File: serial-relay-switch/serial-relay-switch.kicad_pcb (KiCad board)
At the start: 2 copper layers, 170.2 x 66 mm, 75 parts, among them J1 Screw_Terminal_01x01, J10 Screw_Terminal_01x01, J11 Screw_Terminal_01x01, J17 Conn_01x01, J18 Conn_01x01, J19 Screw_Terminal_01x01, J2 2501551-4, J20 Screw_Terminal_01x01, J21 Conn_01x01, J4 Screw_Terminal_01x01, J5 Screw_Terminal_01x01, J6 Screw_Terminal_01x01, J7 Screw_Terminal_01x01, J8 Screw_Terminal_01x01, J9 Screw_Terminal_01x01, K1 G2RL-1-E, K2 G2RL-1-E, K3 G2RL-1-E, K4 G2RL-1-E, K5 G2RL-1-E, K6 G2RL-1-E, K7 G2RL-1-E, K8 G2RL-1-E, U1 H11L1, U13 STM1810T, U14 74LVC1G32, U15 74LVC1G08, U16 74LVC1G04, U17 74LS163, U2 ISL8488E, U3 SZNUD3124DMT1G, U4 ISL8488E, U5 74HC594, U6 SZNUD3124DMT1G, U7 SZNUD3124DMT1G, U8 SZNUD3124DMT1G

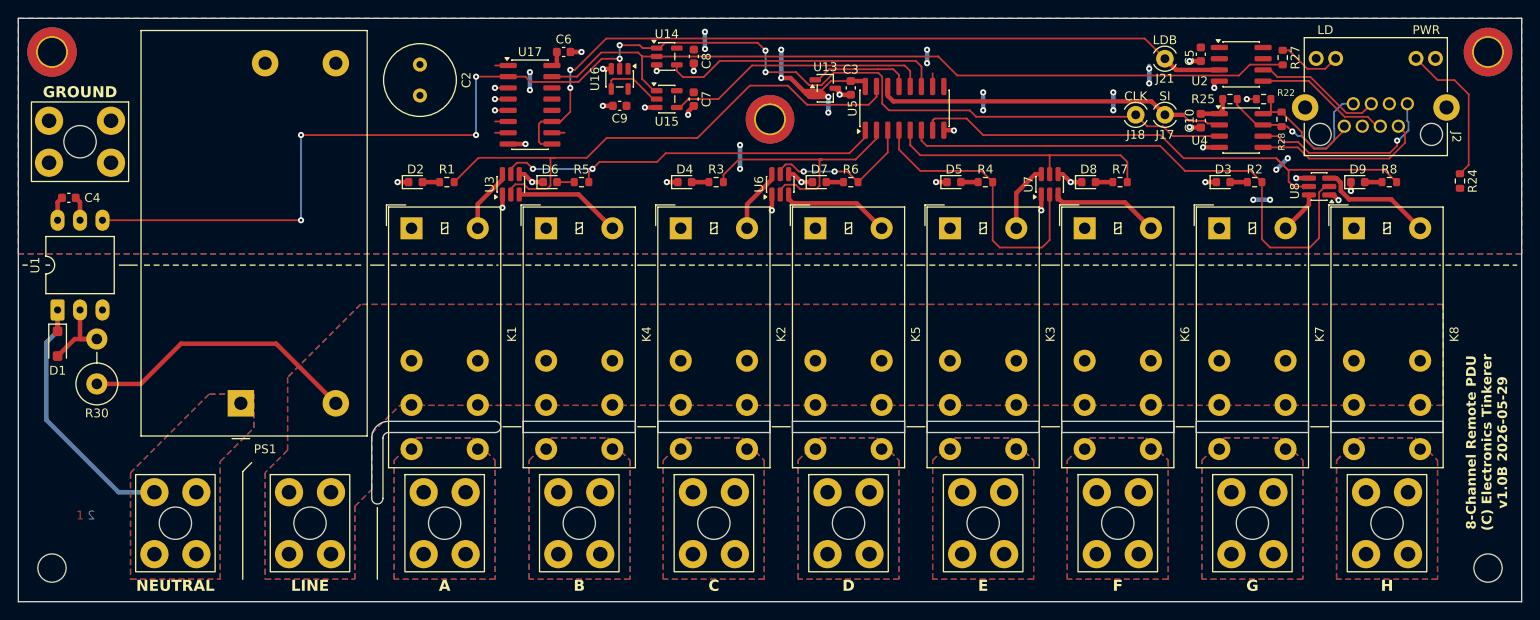
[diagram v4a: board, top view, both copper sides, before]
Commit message: [rs] Add missing pullup on CLK; bump to v1.1A
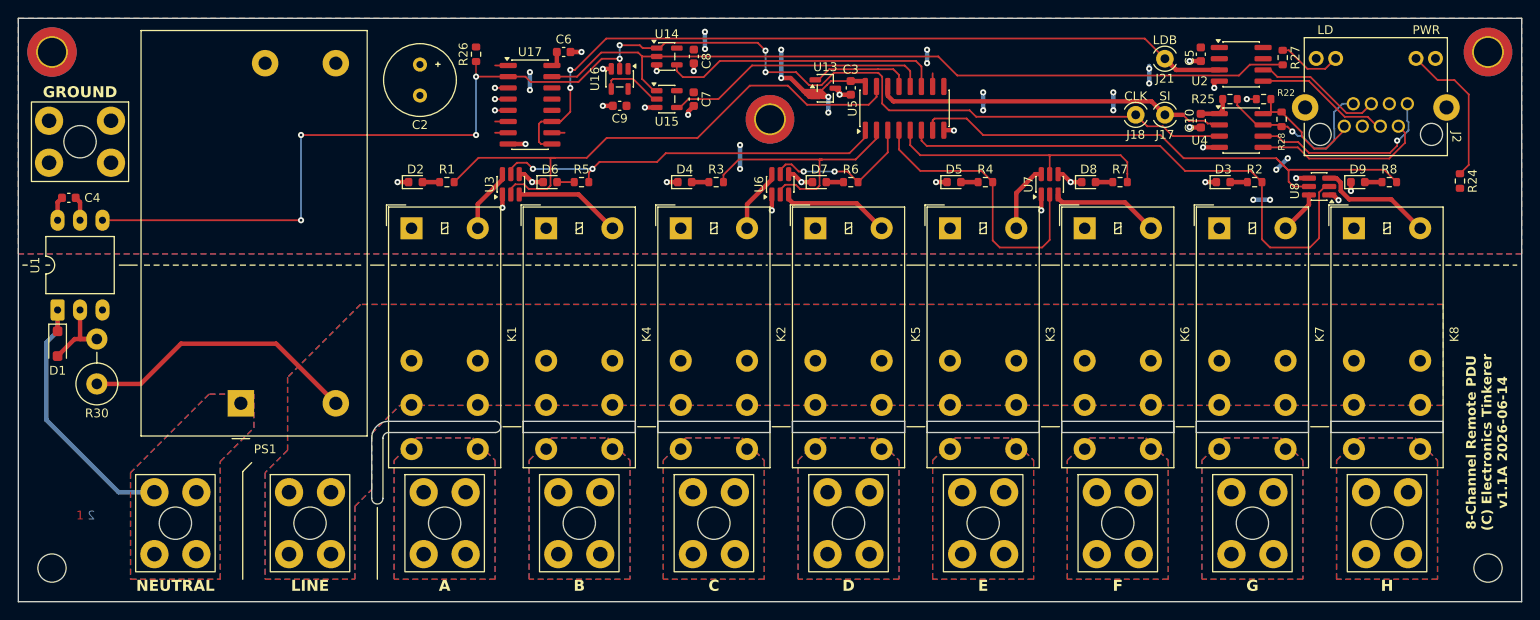
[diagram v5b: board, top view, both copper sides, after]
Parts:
- added R26: 1k, Resistor_SMD:R_0603_1608Metric, F.Cu at (89.6, 46.7)
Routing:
- net /CLK: track 156.0 -> 157.7 mm
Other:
- board text added: "8-Channel Remote PDU (C) Electronics Tinkerer v1.1A 2026-06-14"
- board text removed: "8-Channel Remote PDU (C) Electronics Tinkerer v1.0B 2026-05-29"
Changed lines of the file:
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@@
 		(tags "C Radial series Radial pin pitch 3.50mm diameter 8mm height 7mm Non-Polar Electrolytic Capacitor")
 		(property "Reference" "C2"
-			(at 1.75 -5.25 90)
+			(at 6.83 0 180)
 			(layer "F.SilkS")
 			(effects
@@
 		)
 	)
+	(footprint "Resistor_SMD:R_0603_1608Metric"
+		(layer "F.Cu")
+		(at 89.586 46.674 90)
+		(descr "Resistor SMD 0603 (1608 Metric), square (rectangular) end terminal, IPC-7351 nominal, (Body size source: IPC-SM-782 page 72, https://www.pcb-3d.com/wordpress/wp-content/uploads/ipc-sm-782a_amendment_1_and_2.pdf)")
+		(tags "resistor")
+		(property "Reference" "R26"
+			(at 0 -1.43 90)
+			(layer "F.SilkS")
+			(effects
+				(font
+					(size 1 1)
+					(thickness 0.15)
+				)
+			)
+		)
+		(property "Value" "1k"
+			(at 0 1.43 90)
+			(layer "F.Fab")
+			(effects
+				(font
+					(size 1 1)
+					(thickness 0.15)
+				)
+			)
+		)
+		(property "Datasheet" ""
+			(at 0 0 90)
+			(layer "F.Fab")
+			(hide yes)
+			(effects
+				(font
+					(size 1.27 1.27)
+				)
+			)
+		)
+		(property "Description" ""
+			(at 0 0 90)
+			(layer "F.Fab")
+			(hide yes)
+			(effects
+				(font
+					(size 1.27 1.27)
+				)
+			)
+		)
+		(property "KiLib_Generator" "SMD_2terminal_chip_molded"
+			(at 0 0 90)
+			(layer "F.SilkS")
+			(hide yes)
+			(effects
+				(font
+					(size 1 1)
+					(thickness 0.15)
+				)
+			)
+		)
+		(property ki_fp_filters "R_*")
+		(sheetname "/")
+		(sheetfile "serial-relay-switch.kicad_sch")
+		(units
+			(unit
+				(name "A")
+				(pins "1" "2")
+			)
+		)
+		(attr smd)
+		(duplicate_pad_numbers_are_jumpers no)
+		(fp_line
+			(start -0.237258 -0.5225)
+			(end 0.237258 -0.5225)
+			(stroke
+				(width 0.12)
+				(type solid)
+			)
+			(layer "F.SilkS")
+		)
+		(fp_line
+			(start -0.237258 0.5225)
+			(end 0.237258 0.5225)
+			(stroke
+				(width 0.12)
+				(type solid)
+			)
+			(layer "F.SilkS")
+		)
+		(fp_rect
+			(start -1.48 -0.73)
+			(end 1.48 0.73)
+			(stroke
+				(width 0.05)
+				(type solid)
+			)
+			(fill no)
+			(layer "F.CrtYd")
+		)
+		(fp_rect
+			(start -0.8 -0.4125)
+			(end 0.8 0.4125)
+			(stroke
+				(width 0.1)
+				(type solid)
+			)
+			(fill no)
+			(layer "F.Fab")
+		)
+		(fp_text user "${REFERENCE}"
+			(at 0 0 90)
+			(layer "F.Fab")
+			(effects
+				(font
+					(size 0.4 0.4)
+					(thickness 0.06)
+				)
+			)
+		)
+		(pad "1" smd roundrect
+			(at -0.825 0 90)
+			(size 0.8 0.95)
+			(layers "F.Cu" "F.Mask" "F.Paste")
+			(roundrect_rratio 0.25)
+			(net "/CLK")
+			(pintype "passive")
+		)
+		(pad "2" smd roundrect
+			(at 0.825 0 90)
+			(size 0.8 0.95)
+			(layers "F.Cu" "F.Mask" "F.Paste")
+			(roundrect_rratio 0.25)
+			(net "+5V")
+			(pintype "passive")
+		)
+		(embedded_fonts no)
+		(model "${KICAD10_3DMODEL_DIR}/Resistor_SMD.3dshapes/R_0603_1608Metric.step"
+			(offset
+				(xyz 0 0 0)
+			)
+			(scale
+				(xyz 1 1 1)
+			)
+			(rotate
+				(xyz 0 0 0)
+			)
+		)
+	)
 	(footprint "CUSTOM:ScrewTerminal_Keystone_8195"
 		(layer "F.Cu")
@@
 	)
 	(gr_line
+		(start 85.014 47.817)
+		(end 85.522 47.817)
+		(stroke
+			(width 0.1)
+			(type default)
+		)
+		(layer "F.SilkS")
+	)
+	(gr_line
+		(start 85.268 47.563)
+		(end 85.268 48.071)
+		(stroke
+			(width 0.1)
+			(type default)
+		)
+		(layer "F.SilkS")
+	)
+	(gr_line
 		(start 92.634 70.55)
 		(end 94.666 70.55)
@@
 		)
 	)
-	(gr_text "8-Channel Remote PDU\n(C) Electronics Tinkerer\nv1.0B 2026-05-29"
+	(gr_text "8-Channel Remote PDU\n(C) Electronics Tinkerer\nv1.1A 2026-06-14"
 		(at 201.6 90.616 90)
 		(layer "F.SilkS")
@@
 	)
 	(segment
+		(start 89.586 47.499)
+		(end 89.586 49.214)
+		(width 0.1524)
+		(layer "F.Cu")
+		(net "/CLK")
+	)
+	(segment
 		(start 165.5636 54.8336)
 		(end 167.3416 54.8336)
@@
 	)
 	(zone
+		(net "/SCAN_IN")
+		(layer "F.Cu")
+		(hatch none 0.1)
+		(priority 30001)
+		(attr
+			(teardrop
+				(type padvia)
+			)
+		)
+		(connect_pads yes
+			(clearance 0)
+		)
+		(min_thickness 0.0254)
+		(fill yes
+			(island_removal_mode 1)
+		)
+		(polygon
+			(pts
+				(xy 166.332797 51.941587) (xy 165.973587 52.300797) (xy 166.682079 54.003397) (xy 167.568112 53.536112)
+				(xy 168.035397 52.650079)
+			)
+		)
+	)
+	(zone
 		(net "/LOADB")
 		(layer "F.Cu")
@@
 	)
 	(zone
-		(net "/CLK")
-		(layer "F.Cu")
-		(hatch none 0.1)
-		(priority 30004)
-		(attr
-			(teardrop
-				(type padvia)
-			)
-		)
-		(connect_pads yes
-			(clearance 0)
-		)
-		(min_thickness 0.0254)
-		(fill yes
-			(island_removal_mode 1)
-		)
-		(polygon
-			(pts
-				(xy 165.718045 54.9352) (xy 165.718045 54.732) (xy 165.635442 54.761758) (xy 165.21894 53.241715)
-				(xy 164.257888 53.527888) (xy 163.971715 54.48894) (xy 165.491758 54.905442) (xy 165.5636 54.9352)
-			)
-		)
-	)
-	(zone
-		(net "/SCAN_IN")
+		(net "/LOADB")
 		(layer "F.Cu")
 		(hatch none 0.1)
-		(priority 30000)
+		(priority 30002)
 		(attr
 			(teardrop
@@
 		(polygon
 			(pts
-				(xy 169.559185 53.786) (xy 169.559185 53.278) (xy 167.854285 52.57506) (xy 167.558185 53.532) (xy 167.854285 54.48894)
+				(xy 169.033134 48.706) (xy 169.033134 48.198) (xy 168.834 48.198) (xy 169.013605 48.272395) (xy 168.52094 46.891715)
+				(xy 167.559888 47.177888) (xy 167.273715 48.13894) (xy 168.654395 48.631605) (xy 168.834 48.706)
 			)
 		)
@@
 	)
 	(zone
-		(net "/SCAN_IN")
-		(layer "F.Cu")
-		(hatch none 0.1)
-		(priority 30001)
-		(attr
-			(teardrop
-				(type padvia)
-			)
-		)
-		(connect_pads yes
-			(clearance 0)
-		)
-		(min_thickness 0.0254)
-		(fill yes
-			(island_removal_mode 1)
-		)
-		(polygon
-			(pts
-				(xy 166.332797 51.941587) (xy 165.973587 52.300797) (xy 166.682079 54.003397) (xy 167.568112 53.536112)
-				(xy 168.035397 52.650079)
-			)
-		)
-	)
-	(zone
-		(net "/LOADB")
+		(net "/CLK")
 		(layer "F.Cu")
 		(hatch none 0.1)
-		(priority 30002)
+		(priority 30004)
 		(attr
 			(teardrop
@@
 		(polygon
 			(pts
-				(xy 169.033134 48.706) (xy 169.033134 48.198) (xy 168.834 48.198) (xy 169.013605 48.272395) (xy 168.52094 46.891715)
-				(xy 167.559888 47.177888) (xy 167.273715 48.13894) (xy 168.654395 48.631605) (xy 168.834 48.706)
+				(xy 165.718045 54.9352) (xy 165.718045 54.732) (xy 165.635442 54.761758) (xy 165.21894 53.241715)
+				(xy 164.257888 53.527888) (xy 163.971715 54.48894) (xy 165.491758 54.905442) (xy 165.5636 54.9352)
 			)
 		)
@@
 			)
 		)
+	)
+	(zone
+		(net "/SCAN_IN")
+		(layer "F.Cu")
+		(hatch none 0.1)
+		(priority 30000)
+		(attr
+			(teardrop
+				(type padvia)
+			)
+		)
+		(connect_pads yes
+			(clearance 0)
+		)
+		(min_thickness 0.0254)
+		(fill yes
+			(island_removal_mode 1)
+		)
+		(polygon
+			(pts
+				(xy 169.559185 53.786) (xy 169.559185 53.278) (xy 167.854285 52.57506) (xy 167.558185 53.532) (xy 167.854285 54.48894)
+			)
+		)
